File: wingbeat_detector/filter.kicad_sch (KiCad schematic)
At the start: 2 parts, among them U2 UAF42_SMA, U3 UAF42_SMA

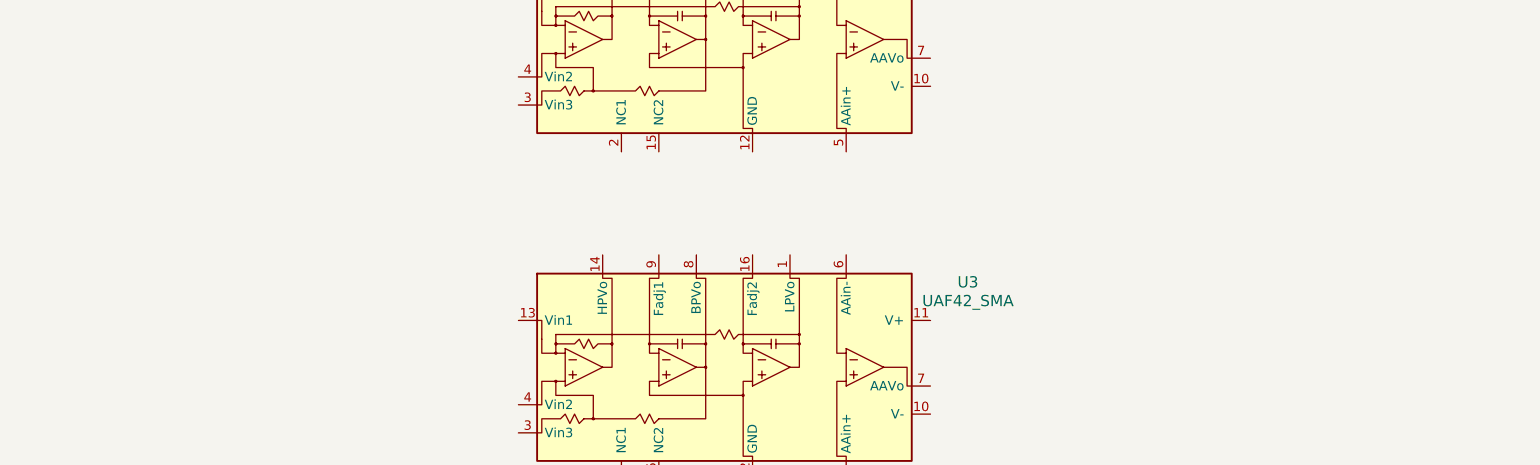
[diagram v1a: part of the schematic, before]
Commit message: Remove connectors schematic sheet
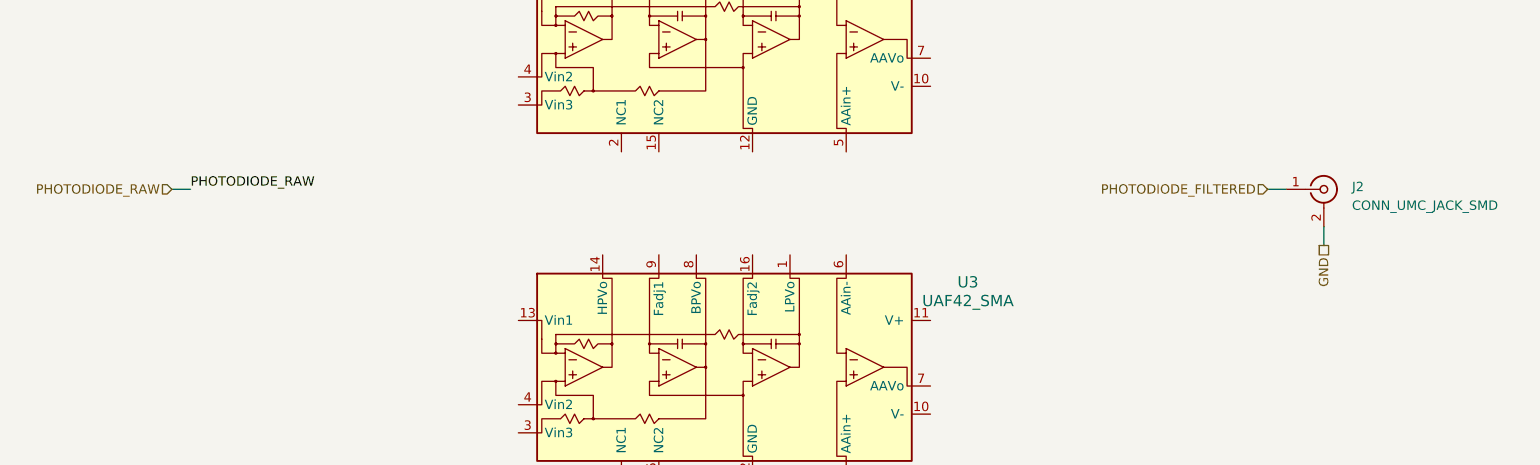
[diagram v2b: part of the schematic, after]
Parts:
- added J2: CONN_UMC_JACK_SMD, Janelia:UMC_AMPHENOL_A-1JB, symbol Janelia:CONN_UMC_JACK_SMD
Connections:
- new net GND: J2.2 (Ext)
- new net PHOTODIODE_FILTERED: J2.1 (In)
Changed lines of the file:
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@@
 (kicad_sch (version 20230121) (generator eeschema)
   (paper "A4")
+  (wire (pts (xy 203.2 96.52) (xy 205.74 96.52))
+    (stroke (width 0) (type default))
+  )
+  (wire (pts (xy 54.61 96.52) (xy 57.15 96.52))
+    (stroke (width 0) (type default))
+  )
+  (wire (pts (xy 210.82 101.6) (xy 210.82 104.14))
+    (stroke (width 0) (type default))
+  )
+  (label "PHOTODIODE_RAW" (at 57.15 96.52 0) (fields_autoplaced)
+    (effects (font (size 1.27 1.27)) (justify left bottom))
+  )
+  (hierarchical_label "PHOTODIODE_FILTERED" (shape input) (at 203.2 96.52 180) (fields_autoplaced)
+    (effects (font (size 1.27 1.27)) (justify right))
+  )
+  (hierarchical_label "GND" (shape passive) (at 210.82 104.14 270) (fields_autoplaced)
+    (effects (font (size 1.27 1.27)) (justify right))
+  )
+  (hierarchical_label "PHOTODIODE_RAW" (shape input) (at 54.61 96.52 180) (fields_autoplaced)
+    (effects (font (size 1.27 1.27)) (justify right))
+  )
   (symbol (lib_id "Janelia:UAF42_SMA") (at 129.54 76.2 0) (unit 1)
     (in_bom yes) (on_board yes) (dnp no) (fields_autoplaced)
@@
         )
         (path "/cc457ebc-4af6-4663-b19f-8cb38f061cb4/6cde90e6-6156-42e3-aaac-c45ad2bfab8b"
-          (reference "U?") (unit 1)
+          (reference "U2") (unit 1)
+        )
+      )
+    )
+  )
+  (symbol (lib_id "Janelia:CONN_UMC_JACK_SMD") (at 210.82 96.52 0) (unit 1)
+    (in_bom yes) (on_board yes) (dnp no) (fields_autoplaced)
+    (property "Reference" "J2" (at 214.63 96.1782 0)
+      (effects (font (size 1.27 1.27)) (justify left))
+    )
+    (property "Value" "CONN_UMC_JACK_SMD" (at 214.63 98.7182 0)
+      (effects (font (size 1.27 1.27)) (justify left))
+    )
+    (property "Footprint" "Janelia:UMC_AMPHENOL_A-1JB" (at 210.82 96.52 0)
+      (effects (font (size 1.27 1.27)) hide)
+    )
+    (property "Datasheet" "" (at 210.82 96.52 0)
+      (effects (font (size 1.27 1.27)) hide)
+    )
+    (property "Manufacturer" "Amphenol RF" (at 210.82 96.52 0)
+      (effects (font (size 1.27 1.27)) hide)
+    )
+    (property "Manufacturer Part Number" "A-1JB" (at 210.82 96.52 0)
+      (effects (font (size 1.27 1.27)) hide)
+    )
+    (property "Vendor" "Digi-Key" (at 210.82 96.52 0)
+      (effects (font (size 1.27 1.27)) hide)
+    )
+    (property "Vendor Part Number" "115-A-1JBCT-ND" (at 210.82 96.52 0)
+      (effects (font (size 1.27 1.27)) hide)
+    )
+    (property "Description" "CONN UMC JACK STR 50 OHM SMD" (at 213.36 99.9882 0)
+      (effects (font (size 1.27 1.27)) (justify left) hide)
+    )
+    (pin "1")
+    (pin "2")
+    (instances
+      (project "wingbeat_detector"
+        (path "/cc457ebc-4af6-4663-b19f-8cb38f061cb4"
+          (reference "J2") (unit 1)
+        )
+        (path "/cc457ebc-4af6-4663-b19f-8cb38f061cb4/6cde90e6-6156-42e3-aaac-c45ad2bfab8b"
+          (reference "J2") (unit 1)
         )
       )
@@
         )
         (path "/cc457ebc-4af6-4663-b19f-8cb38f061cb4/6cde90e6-6156-42e3-aaac-c45ad2bfab8b"
-          (reference "U?") (unit 1)
+          (reference "U3") (unit 1)
         )
       )

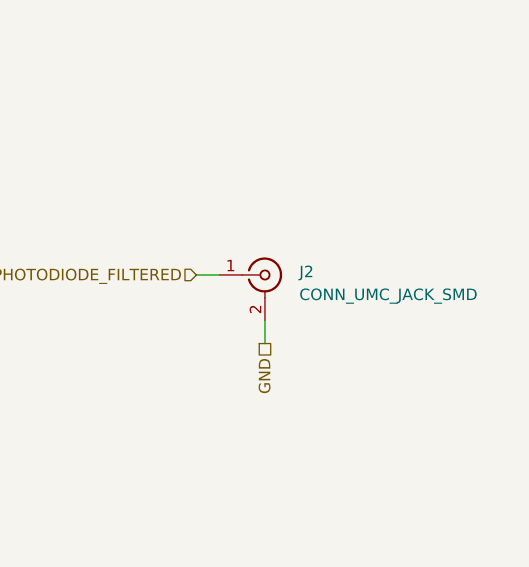
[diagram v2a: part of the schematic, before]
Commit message: Add buffered output
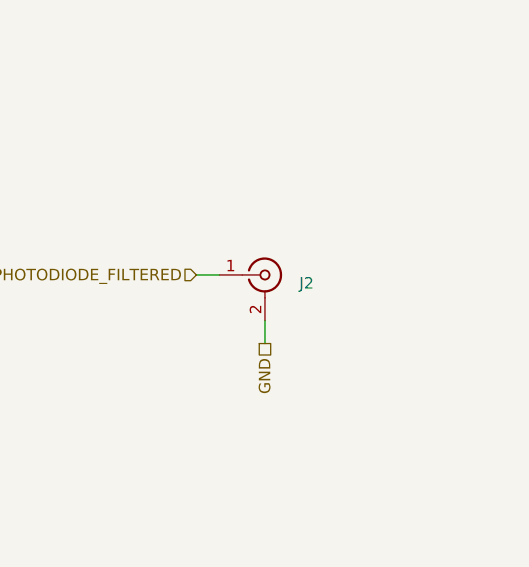
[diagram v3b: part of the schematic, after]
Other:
- company: (none) -> Howard Hughes Medical Institute
- title: (none) -> wingbeat_detector
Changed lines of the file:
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@@
 (kicad_sch (version 20230121) (generator eeschema)
   (paper "A4")
+  (title_block
+    (title "wingbeat_detector")
+    (rev "3.0")
+    (company "Howard Hughes Medical Institute")
+  )
   (wire (pts (xy 203.2 96.52) (xy 205.74 96.52))
     (stroke (width 0) (type default))
@@
   (symbol (lib_id "Janelia:CONN_UMC_JACK_SMD") (at 210.82 96.52 0) (unit 1)
     (in_bom yes) (on_board yes) (dnp no) (fields_autoplaced)
-    (property "Reference" "J2" (at 214.63 96.1782 0)
+    (property "Reference" "J2" (at 214.63 97.4482 0)
       (effects (font (size 1.27 1.27)) (justify left))
     )
-    (property "Value" "CONN_UMC_JACK_SMD" (at 214.63 98.7182 0)
-      (effects (font (size 1.27 1.27)) (justify left))
+    (property "Value" "CONN_UMC_JACK_SMD" (at 213.741 96.52 90)
+      (effects (font (size 1.27 1.27)) hide)
     )
-    (property "Footprint" "Janelia:UMC_AMPHENOL_A-1JB" (at 210.82 96.52 0)
+    (property "Footprint" "Janelia:UMC_AMPHENOL_A-1JB" (at 210.82 83.82 0)
       (effects (font (size 1.27 1.27)) hide)
     )
@@
       (effects (font (size 1.27 1.27)) hide)
     )
-    (property "Manufacturer" "Amphenol RF" (at 210.82 96.52 0)
+    (property "Manufacturer" "Amphenol RF" (at 210.82 86.36 0)
       (effects (font (size 1.27 1.27)) hide)
     )
-    (property "Manufacturer Part Number" "A-1JB" (at 210.82 96.52 0)
+    (property "Manufacturer Part Number" "A-1JB" (at 210.82 111.76 0)
       (effects (font (size 1.27 1.27)) hide)
     )
-    (property "Vendor" "Digi-Key" (at 210.82 96.52 0)
+    (property "Vendor" "Digi-Key" (at 210.82 114.3 0)
       (effects (font (size 1.27 1.27)) hide)
     )
-    (property "Vendor Part Number" "115-A-1JBCT-ND" (at 210.82 96.52 0)
+    (property "Vendor Part Number" "115-A-1JBCT-ND" (at 210.82 109.22 0)
       (effects (font (size 1.27 1.27)) hide)
     )
-    (property "Description" "CONN UMC JACK STR 50 OHM SMD" (at 213.36 99.9882 0)
-      (effects (font (size 1.27 1.27)) (justify left) hide)
+    (property "Description" "CONN UMC JACK STR 50 OHM SMD" (at 210.82 81.28 0)
+      (effects (font (size 1.27 1.27)) hide)
     )
     (pin "1")

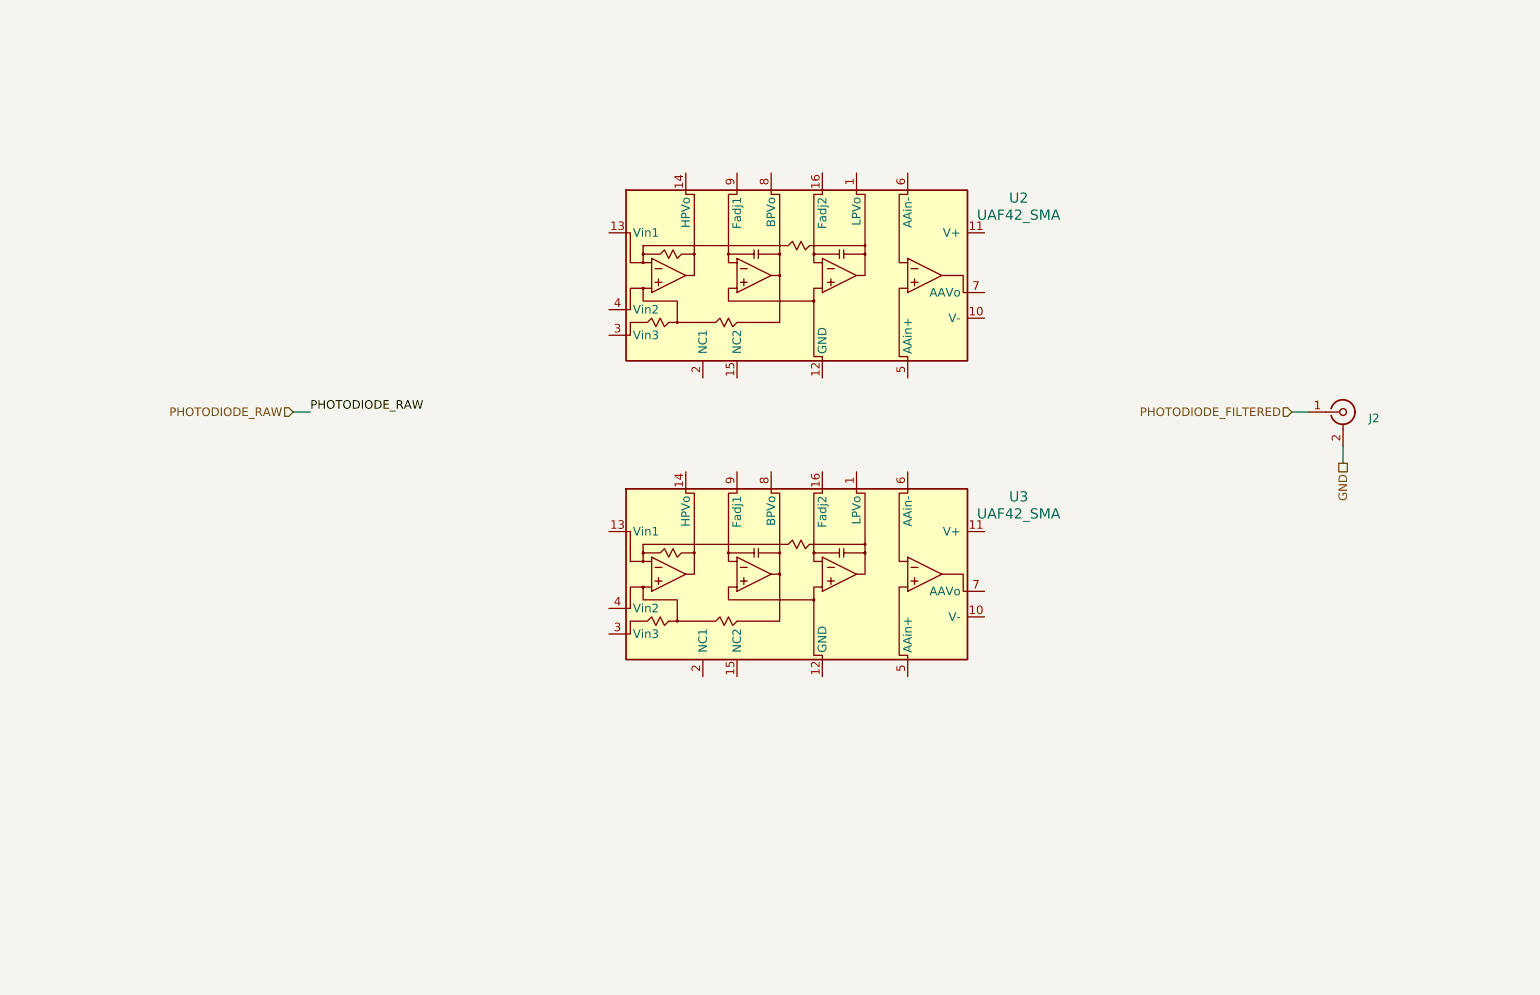
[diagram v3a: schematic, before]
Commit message: Initial schematic layout
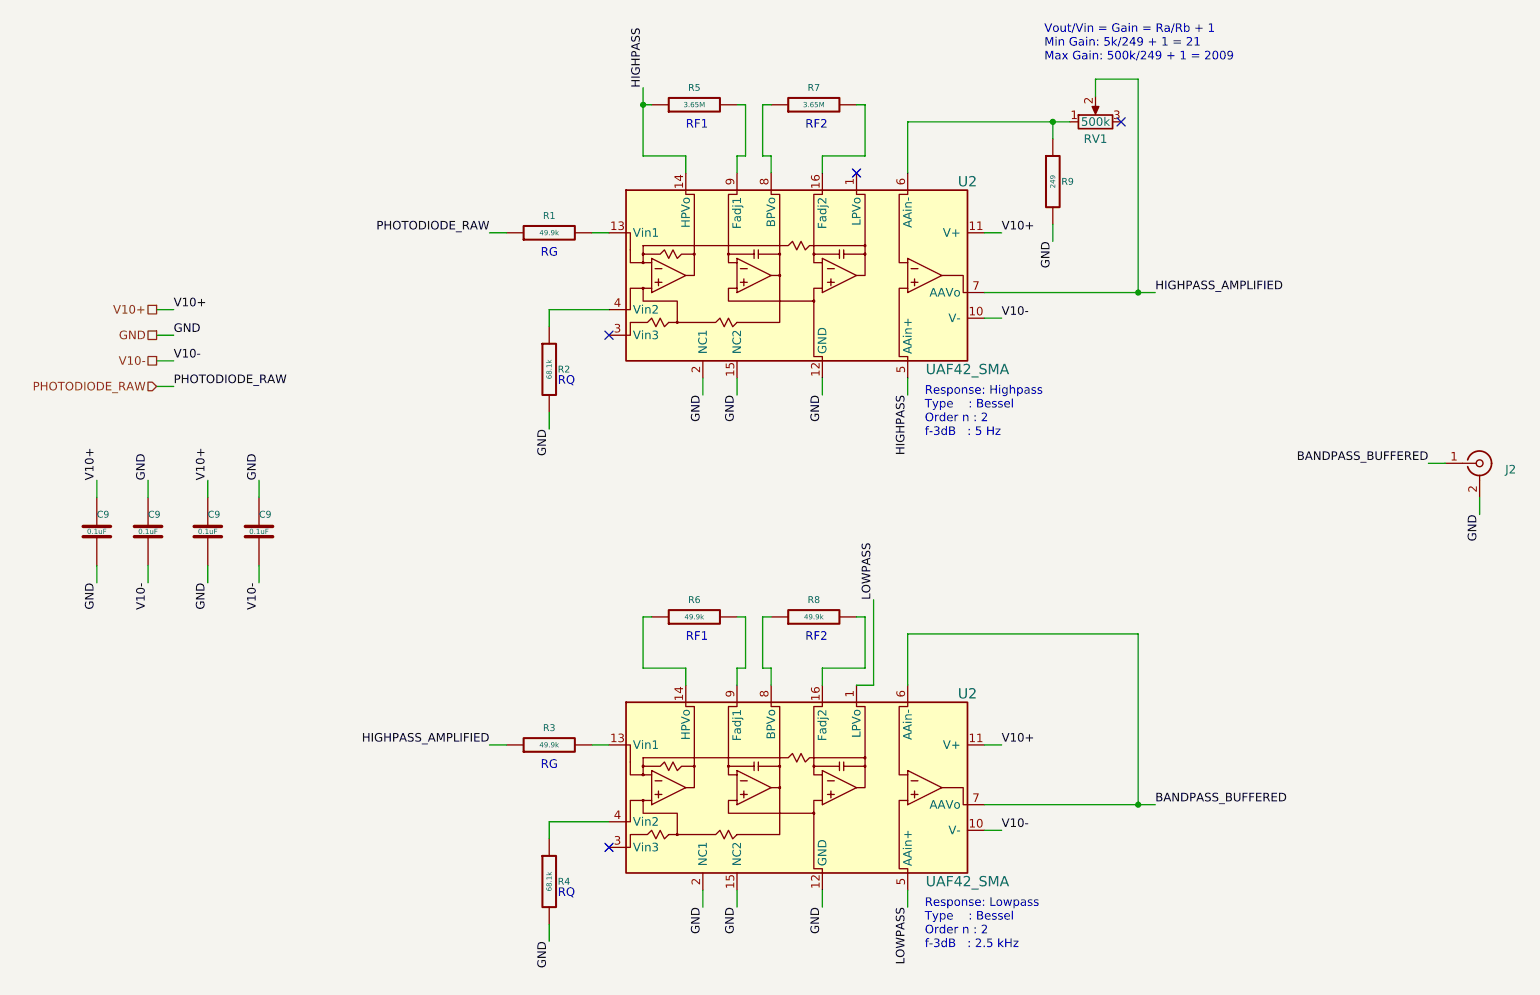
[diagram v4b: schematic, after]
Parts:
- removed U3: UAF42_SMA, Janelia:SOIC-16W_7.5x10.3mm_P1.27mm, symbol Janelia:UAF42_SMA
- added C9 (x4): 0.1uF, Janelia:C_0402_1005Metric, symbol Janelia:C_0.1uF_0402
- added R1, R3, R6, R8: 49.9k, Janelia:R_0402_1005Metric, symbol Janelia:R_49.9k_0402
- added R2, R4: 68.1k, Janelia:R_0402_1005Metric, symbol Janelia:R_68.1k_0402
- added R5, R7: 3.65M, Janelia:R_0603_1608Metric, symbol Janelia:R_3.65M_0603
- added R9: 249, Janelia:R_0402_1005Metric, symbol Janelia:R_249_0402
- added RV1: 500k, Janelia:Potentiometer_Bourns_3223W_Vertical, symbol Janelia:R_Potentiometer_500k_3.9x3.18mm_11turn_Vertical
- added U2: UAF42_SMA, Janelia:SOIC-16W_7.5x10.3mm_P1.27mm, symbol Janelia:UAF42_SMA
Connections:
- net GND: now also U2.12 (GND), U2.15 (NC2), U2.2 (NC1), C9.1, C9.1, C9.2, C9.2, R2.2, R4.2, R9.2, U2.12 (GND), U2.15 (NC2), U2.2 (NC1)
- net PHOTODIODE_RAW: now also R1.1
- net V10-: now reaches U2.10 (V-)
- net V10-: now also C9.2, C9.2, U2.10 (V-)
- net V10+: now reaches U2.11 (V+)
- net V10+: now also C9.1, C9.1, U2.11 (V+)
- net at U2.13 (Vin1): now also R1.2
- net HIGHPASS: now reaches U2.14 (HPVo)
- net HIGHPASS: now also U2.5 (AAin+), R5.1
- net at U2.16 (Fadj2): now also R7.2
- net at U2.4 (Vin2): now also R2.1
- net at U2.6 (AAin-): now also R9.1, RV1.1
- net HIGHPASS_AMPLIFIED: now reaches U2.7 (AAVo)
- net HIGHPASS_AMPLIFIED: now also R3.1, RV1.2
- net at U2.8 (BPVo): now also R7.1
- net at U2.9 (Fadj1): now also R5.2
- net PHOTODIODE_FILTERED renamed BANDPASS_BUFFERED
- net BANDPASS_BUFFERED: now also U2.6 (AAin-), U2.7 (AAVo)
- new net: R3.2, U2.13 (Vin1)
- new net: R6.1, U2.14 (HPVo)
- new net: R8.2, U2.16 (Fadj2)
- new net: R4.1, U2.4 (Vin2)
- new net: R8.1, U2.8 (BPVo)
- new net: R6.2, U2.9 (Fadj1)
- new net LOWPASS: U2.1 (LPVo), U2.5 (AAin+)
- no-connect marks 0 -> 4
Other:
- note added: "RF1"
- note added: "RF2"
- note added: "RG"
- note added: "RQ"
- note added: "Response: Highpass Type : Bessel Order n : 2 f-3dB : 5 Hz"
- note added: "Response: Lowpass Type : Bessel Order n : 2 f-3dB : 2.5 kHz"
- note added: "Vout/Vin = Gain = Ra/Rb + 1 Min Gain: 5k/249 + 1 = 21 Max Gain: 500k/249 + 1 = 2009"
- moved on the sheet: J2

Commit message: Double check schematic
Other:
- moved on the sheet: C9
